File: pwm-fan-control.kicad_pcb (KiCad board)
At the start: 2 copper layers, 38.5 x 19 mm, 25 parts, among them J1 Fan-out0, J2 PWM and power, J3 Fan-out1, Q1 Q_NMOS_GSD, Q2 Q_NMOS_GSD, U1 LM358

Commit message: Flipped some stuff for symetry
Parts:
- moved R6 11.6 mm to (224.8, 56.0)
- moved Q1 2.40 mm to (232.0, 56.9), turned to 180 degrees
- moved C3 1.60 mm to (219.2, 45.6)
- moved R9 1.60 mm to (219.2, 47.2)
- moved R10 1.21 mm to (222.7, 50.1), turned to 270 degrees
- moved REF** 1.00 mm to (243.5, 61.0)
- moved R3 0.52 mm to (222.7, 55.2)
- moved R12 0.40 mm to (224.8, 49.2)
- turned R11 to 270 degrees
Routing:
- net Net-(J1-Pad1): track 22.6 -> 3.56 mm
- net Net-(Q1-Pad1): track 3.91 -> 22.9 mm
- net GND: track 59.8 -> 51.0 mm, vias 12 -> 23
- net Net-(R11-Pad2): track 12.1 -> 5.14 mm
- net Net-(Q1-Pad2): track 18.8 -> 15.6 mm
- net Net-(Q2-Pad1): track 15.0 -> 17.7 mm
- net Net-(J3-Pad1): track 4.83 -> 3.75 mm
- net Net-(Q2-Pad2): track 12.3 -> 11.4 mm
- net /~PWM1: track 14.9 -> 15.8 mm
- net Net-(R3-Pad2): track 9.93 -> 9.09 mm
- net Net-(R10-Pad2): track 7.19 -> 6.42 mm

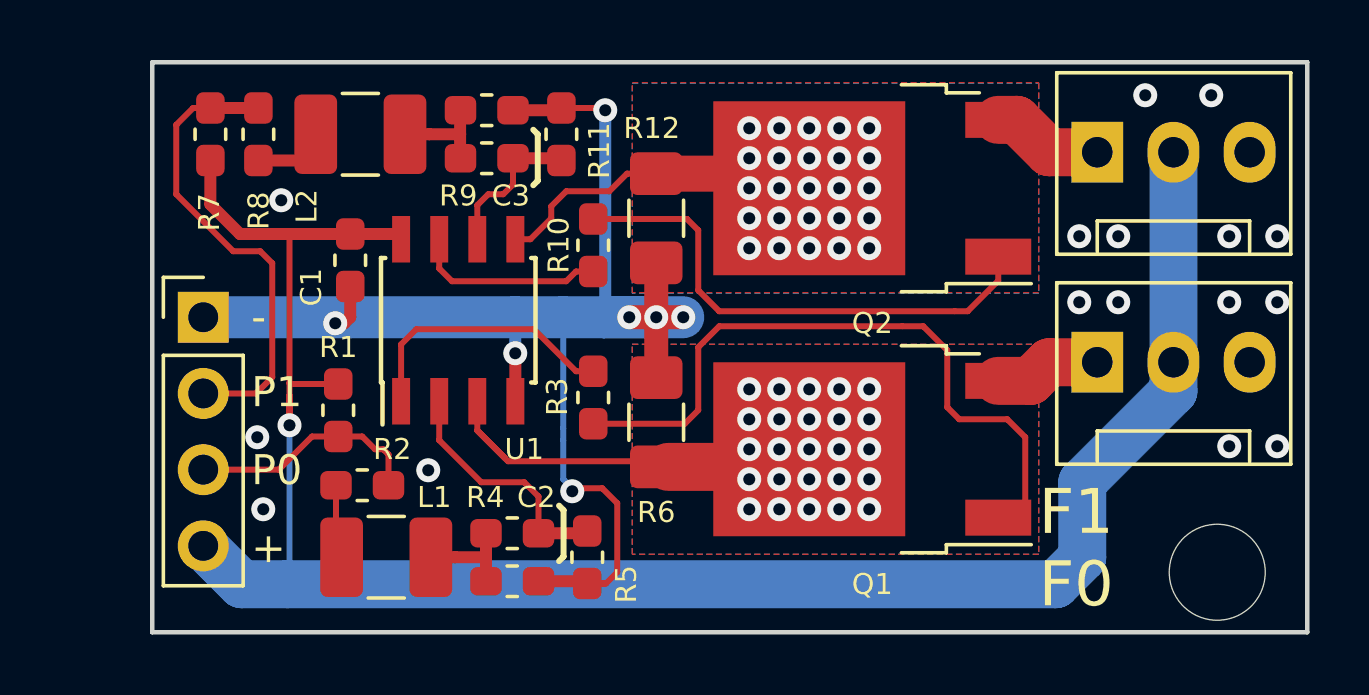
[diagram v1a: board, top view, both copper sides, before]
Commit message: Un-inverted PWM input
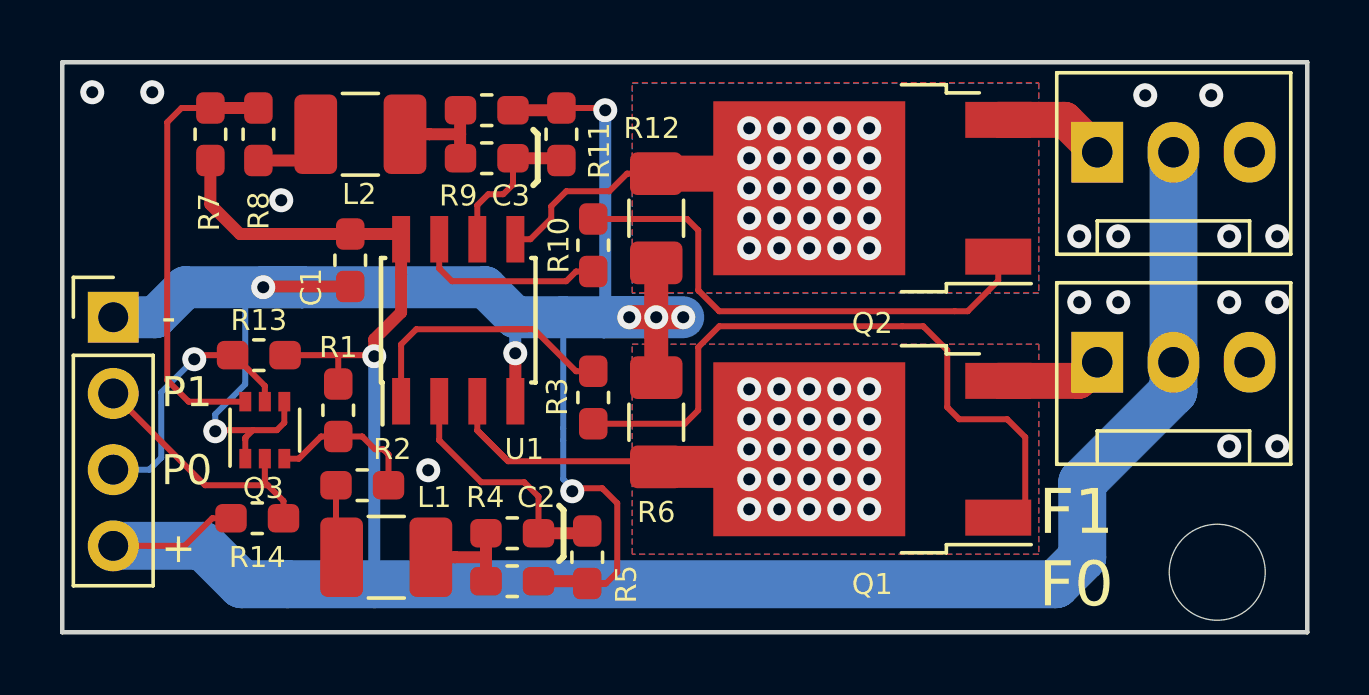
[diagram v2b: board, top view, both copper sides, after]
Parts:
- added Q3: MUN5211DW1, Package_TO_SOT_SMD:SOT-363_SC-70-6, F.Cu at (211.8, 56.3)
- added R13: 10k, Resistor_SMD:R_0603_1608Metric_Pad1.05x0.95mm_HandSolder, F.Cu at (211.6, 53.8)
- added R14: 10k, Resistor_SMD:R_0603_1608Metric_Pad1.05x0.95mm_HandSolder, F.Cu at (211.5, 59.2)
- moved J2 3.00 mm to (206.7, 52.5)
- moved G*** 0.34 mm to (216.4, 49.2)
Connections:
- R1 pad 1: /~PWM0 -> /PWM0
- R2 pad 2: /~PWM0 -> /PWM0
- R7 pad 1: /~PWM1 -> /PWM1
- R8 pad 2: /~PWM1 -> /PWM1
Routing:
- net GND: track 51.0 -> 67.0 mm, vias 23 -> 24
- net /PWM1: track 0.00 -> 14.7 mm
- net VCCFan: track 67.6 -> 76.8 mm
- net /~PWM1: track 15.8 -> 8.66 mm
- net /PWM0: track 0.00 -> 5.05 mm
- net /~PWM0: track 7.91 -> 8.86 mm, vias 0 -> 1
- net Net-(R3-Pad2): track 9.09 -> 9.89 mm
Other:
- board size 38.5 x 19 mm -> 41.5 x 19 mm
